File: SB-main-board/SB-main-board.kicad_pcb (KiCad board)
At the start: 4 copper layers, 53 x 40 mm, 93 parts, among them J1 XT30PB_IN, J2 USB_C_Receptacle_USB2.0_16P, J3 Excluder, J4 PT100, J5 Hotend, J6 FAN2, J7 LDC, J8 FS, J9 FAN, Q1 BUK9M8R5-40EX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

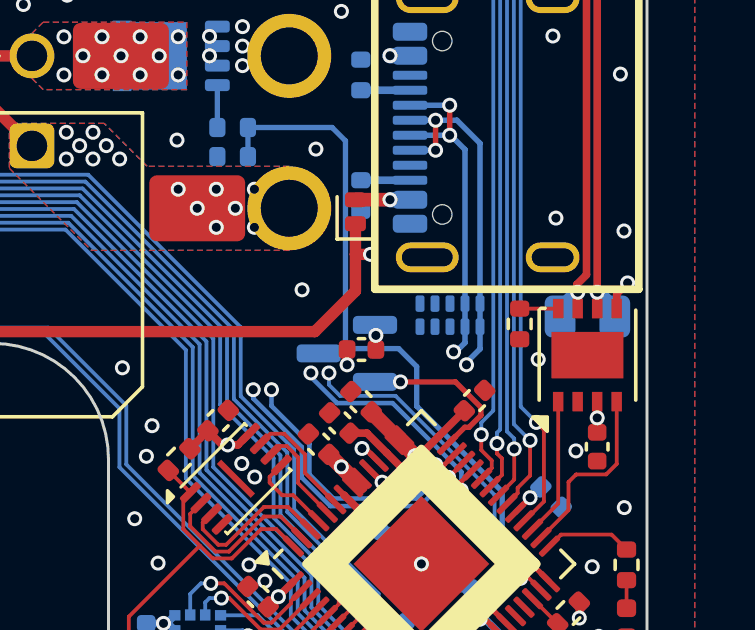
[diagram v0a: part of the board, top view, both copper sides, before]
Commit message: layout: change the tvs to 0522
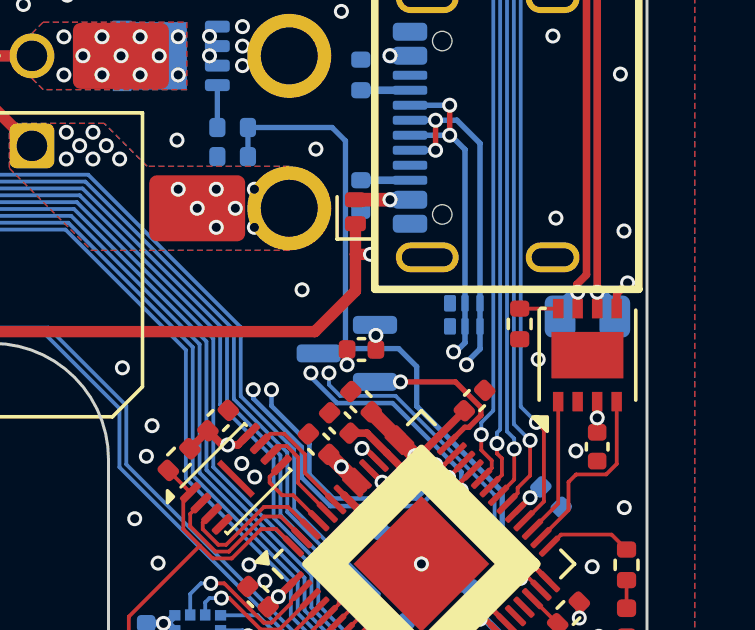
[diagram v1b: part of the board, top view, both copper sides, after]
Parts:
- D3: value TPD4E02B04DQA -> RCLAMP0522P; footprint Package_SON:USON-10_2.5x1.0mm_P0.5mm -> Library:SLP1610P4
- moved D3 0.50 mm to (119.3, 91.4), turned to 90 degrees
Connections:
- D3 pad 1: unconnected-(D3-IO1-Pad1) -> /USB_D+
- D3 pad 2: unconnected-(D3-IO2-Pad2) -> /USB_D-
- D3 pad 4: /USB_D- -> GND
- D3 pad 5: /USB_D+ -> /USB_D-

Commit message: change bom
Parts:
- Q1: value BUK9M8R5-40EX -> BUK9M4R3-40H
- R15: value 11mR -> 200mR
- R16: value 11mR -> 220mR
- U10: value TMP235A2 -> LM50
- U6: value TMC2208-LA -> TMC2209-LA

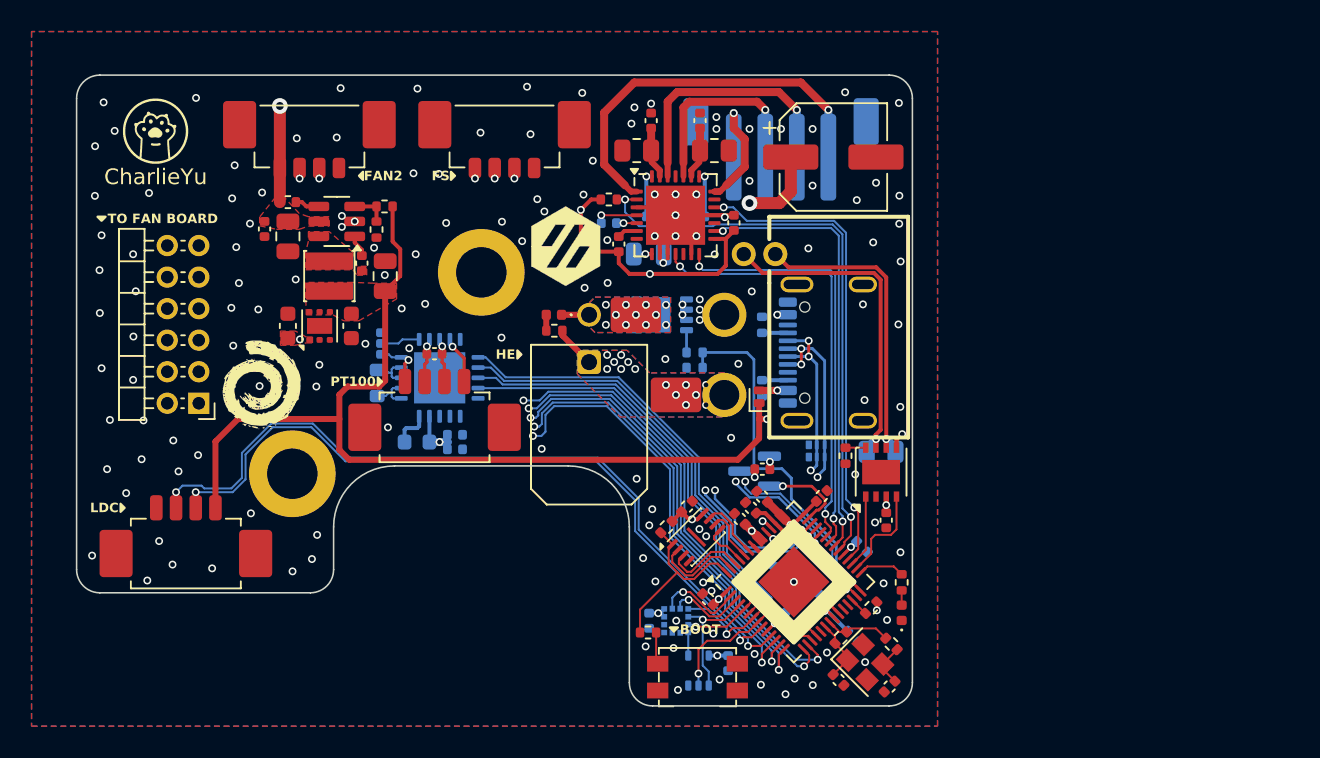
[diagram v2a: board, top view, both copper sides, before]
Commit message: layout: optmise routes
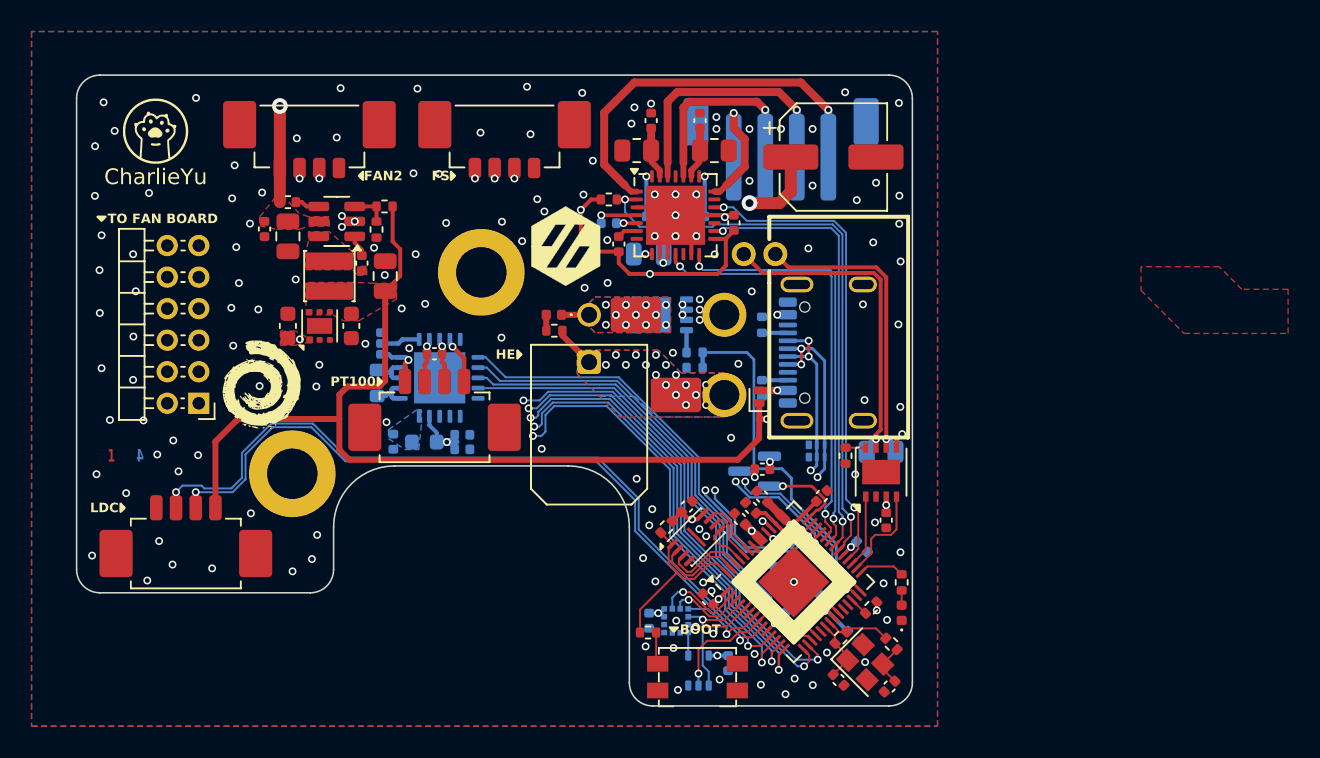
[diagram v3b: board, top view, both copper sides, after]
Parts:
- added C36: 100nF, Capacitor_SMD:C_0402_1005Metric, B.Cu at (92.5, 90.8)
- J2: value USB_C_Receptacle_USB2.0_16P -> Download
- moved C31 0.46 mm to (96.9, 90.4)
- moved C32 0.46 mm to (96.9, 91.3)
- moved FB1 0.46 mm to (94.5, 90.9)
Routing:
- net Net-(U9-VDD): track 2.23 -> 0.00 mm
- net +24V: vias 18 -> 20
- added copper zone on In2.Cu, net +24V
- added copper zone on B.Cu, net Net-(U9-VDD)
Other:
- board text added: "2"
- board text added: "3"
- board text added: "Close upper jumpper when using 2W/4W or Close the lower one"
- board text removed: "4W"
